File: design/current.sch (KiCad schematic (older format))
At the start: 4 parts

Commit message: Fixing connection errors
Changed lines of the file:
@@
 AR Path="/548DF2C8/55B3BD79/55B231D6" Ref="R30"  Part="1"
 AR Path="/548DF2C8/55B3BD84/55B231D6" Ref="R33"  Part="1"
-F 0 "R27" V 3605 2675 50  0000 C CNN
+F 0 "R33" V 3605 2675 50  0000 C CNN
 F 1 "22R" V 3525 2675 50  0000 C CNN
 F 2 "Resistors_SMD:R_0603" V 3455 2675 30  0001 C CNN
@@
 AR Path="/548DF2C8/55B3BD79/55B23207" Ref="R31"  Part="1"
 AR Path="/548DF2C8/55B3BD84/55B23207" Ref="R34"  Part="1"
-F 0 "R28" V 4080 2675 50  0000 C CNN
+F 0 "R34" V 4080 2675 50  0000 C CNN
 F 1 "10K" V 4000 2675 50  0000 C CNN
 F 2 "Resistors_SMD:R_0603" V 3930 2675 30  0001 C CNN
@@
 AR Path="/548DF2C8/55B3BD79/55B23290" Ref="R32"  Part="1"
 AR Path="/548DF2C8/55B3BD84/55B23290" Ref="R35"  Part="1"
-F 0 "R29" V 4080 3175 50  0000 C CNN
+F 0 "R35" V 4080 3175 50  0000 C CNN
 F 1 "10K" V 4000 3175 50  0000 C CNN
 F 2 "Resistors_SMD:R_0603" V 3930 3175 30  0001 C CNN
@@
 AR Path="/548DF2C8/55B3BD79/55B232D0" Ref="C6"  Part="1"
 AR Path="/548DF2C8/55B3BD84/55B232D0" Ref="C7"  Part="1"
-F 0 "C5" H 3550 3275 50  0000 L CNN
+F 0 "C7" H 3550 3275 50  0000 L CNN
 F 1 "10uF" H 3550 3075 50  0000 L CNN
 F 2 "Capacitors_SMD:C_0805" H 3563 3025 30  0001 C CNN
@@
 Connection ~ 4000 2875
 $Comp
-L GND #PWR053
+L GND #PWR054
 U 1 1 55B23417
 P 3525 3375
-AR Path="/548DF2C8/55B266EE/55B23417" Ref="#PWR053"  Part="1"
-AR Path="/548DF2C8/55B3A3F6/55B23417" Ref="#PWR055"  Part="1"
-AR Path="/548DF2C8/55B3A74F/55B23417" Ref="#PWR057"  Part="1"
-AR Path="/548DF2C8/55B3BD6E/55B23417" Ref="#PWR059"  Part="1"
-AR Path="/548DF2C8/55B3BD79/55B23417" Ref="#PWR061"  Part="1"
-AR Path="/548DF2C8/55B3BD84/55B23417" Ref="#PWR063"  Part="1"
-F 0 "#PWR059" H 3525 3125 50  0001 C CNN
+AR Path="/548DF2C8/55B266EE/55B23417" Ref="#PWR054"  Part="1"
+AR Path="/548DF2C8/55B3A3F6/55B23417" Ref="#PWR056"  Part="1"
+AR Path="/548DF2C8/55B3A74F/55B23417" Ref="#PWR058"  Part="1"
+AR Path="/548DF2C8/55B3BD6E/55B23417" Ref="#PWR060"  Part="1"
+AR Path="/548DF2C8/55B3BD79/55B23417" Ref="#PWR062"  Part="1"
+AR Path="/548DF2C8/55B3BD84/55B23417" Ref="#PWR064"  Part="1"
+F 0 "#PWR064" H 3525 3125 50  0001 C CNN
 F 1 "GND" H 3525 3225 50  0000 C CNN
 F 2 "" H 3525 3375 60  0000 C CNN
@@
 	4000 2525 4000 2475
 $Comp
-L +3.3V #PWR054
+L +3.3V #PWR055
 U 1 1 55B23695
 P 4000 2475
-AR Path="/548DF2C8/55B266EE/55B23695" Ref="#PWR054"  Part="1"
-AR Path="/548DF2C8/55B3A3F6/55B23695" Ref="#PWR056"  Part="1"
-AR Path="/548DF2C8/55B3A74F/55B23695" Ref="#PWR058"  Part="1"
-AR Path="/548DF2C8/55B3BD6E/55B23695" Ref="#PWR060"  Part="1"
-AR Path="/548DF2C8/55B3BD79/55B23695" Ref="#PWR062"  Part="1"
-AR Path="/548DF2C8/55B3BD84/55B23695" Ref="#PWR064"  Part="1"
-F 0 "#PWR060" H 4000 2325 50  0001 C CNN
+AR Path="/548DF2C8/55B266EE/55B23695" Ref="#PWR055"  Part="1"
+AR Path="/548DF2C8/55B3A3F6/55B23695" Ref="#PWR057"  Part="1"
+AR Path="/548DF2C8/55B3A74F/55B23695" Ref="#PWR059"  Part="1"
+AR Path="/548DF2C8/55B3BD6E/55B23695" Ref="#PWR061"  Part="1"
+AR Path="/548DF2C8/55B3BD79/55B23695" Ref="#PWR063"  Part="1"
+AR Path="/548DF2C8/55B3BD84/55B23695" Ref="#PWR065"  Part="1"
+F 0 "#PWR065" H 4000 2325 50  0001 C CNN
 F 1 "+3.3V" H 4000 2615 50  0000 C CNN
 F 2 "" H 4000 2475 60  0000 C CNN

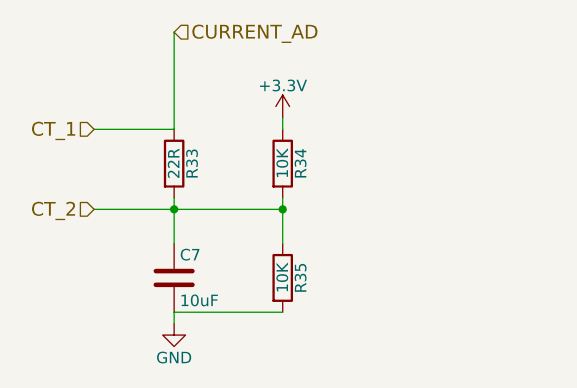
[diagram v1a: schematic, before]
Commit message: Agrego los dos circuitos extra para medir tension
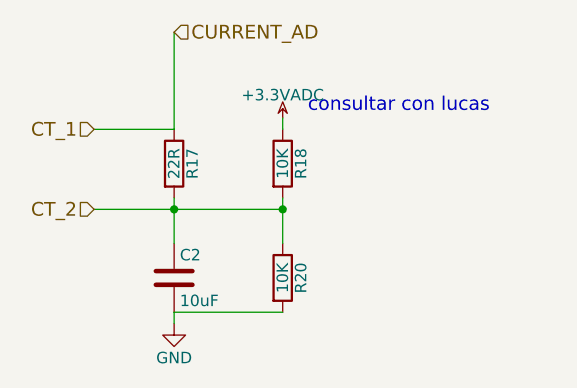
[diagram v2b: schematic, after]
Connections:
- net +3V3 renamed +3.3VADC
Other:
- note added: "consultar con lucas\n"
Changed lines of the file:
@@
 LIBS:memory
 LIBS:xilinx
-LIBS:special
 LIBS:microcontrollers
 LIBS:dsp
@@
 $Descr A4 11693 8268
 encoding utf-8
-Sheet 13 18
+Sheet 13 20
 Title "PIVI"
 Date "Mon 27 Jul 2015"
@@
 AR Path="/548DF2C8/55B3BD79/55B231D6" Ref="R30"  Part="1"
 AR Path="/548DF2C8/55B3BD84/55B231D6" Ref="R33"  Part="1"
-F 0 "R33" V 3605 2675 50  0000 C CNN
+F 0 "R17" V 3605 2675 50  0000 C CNN
 F 1 "22R" V 3525 2675 50  0000 C CNN
 F 2 "Resistors_SMD:R_0603" V 3455 2675 30  0001 C CNN
@@
 AR Path="/548DF2C8/55B3BD79/55B23207" Ref="R31"  Part="1"
 AR Path="/548DF2C8/55B3BD84/55B23207" Ref="R34"  Part="1"
-F 0 "R34" V 4080 2675 50  0000 C CNN
+F 0 "R18" V 4080 2675 50  0000 C CNN
 F 1 "10K" V 4000 2675 50  0000 C CNN
 F 2 "Resistors_SMD:R_0603" V 3930 2675 30  0001 C CNN
@@
 AR Path="/548DF2C8/55B3BD79/55B23290" Ref="R32"  Part="1"
 AR Path="/548DF2C8/55B3BD84/55B23290" Ref="R35"  Part="1"
-F 0 "R35" V 4080 3175 50  0000 C CNN
+F 0 "R20" V 4080 3175 50  0000 C CNN
 F 1 "10K" V 4000 3175 50  0000 C CNN
 F 2 "Resistors_SMD:R_0603" V 3930 3175 30  0001 C CNN
@@
 AR Path="/548DF2C8/55B3BD79/55B232D0" Ref="C6"  Part="1"
 AR Path="/548DF2C8/55B3BD84/55B232D0" Ref="C7"  Part="1"
-F 0 "C7" H 3550 3275 50  0000 L CNN
+F 0 "C2" H 3550 3275 50  0000 L CNN
 F 1 "10uF" H 3550 3075 50  0000 L CNN
 F 2 "Capacitors_SMD:C_0805" H 3563 3025 30  0001 C CNN
@@
 AR Path="/548DF2C8/55B3BD79/55B23417" Ref="#PWR062"  Part="1"
 AR Path="/548DF2C8/55B3BD84/55B23417" Ref="#PWR064"  Part="1"
-F 0 "#PWR064" H 3525 3125 50  0001 C CNN
+F 0 "#PWR054" H 3525 3125 50  0001 C CNN
 F 1 "GND" H 3525 3225 50  0000 C CNN
 F 2 "" H 3525 3375 60  0000 C CNN
@@
 Wire Wire Line
 	4000 2525 4000 2475
+Wire Wire Line
+	3525 3325 4000 3325
 $Comp
-L +3.3V #PWR055
-U 1 1 55B23695
+L +3.3VADC #PWR?
+U 1 1 55B9DD7E
 P 4000 2475
-AR Path="/548DF2C8/55B266EE/55B23695" Ref="#PWR055"  Part="1"
-AR Path="/548DF2C8/55B3A3F6/55B23695" Ref="#PWR057"  Part="1"
-AR Path="/548DF2C8/55B3A74F/55B23695" Ref="#PWR059"  Part="1"
-AR Path="/548DF2C8/55B3BD6E/55B23695" Ref="#PWR061"  Part="1"
-AR Path="/548DF2C8/55B3BD79/55B23695" Ref="#PWR063"  Part="1"
-AR Path="/548DF2C8/55B3BD84/55B23695" Ref="#PWR065"  Part="1"
-F 0 "#PWR065" H 4000 2325 50  0001 C CNN
-F 1 "+3.3V" H 4000 2615 50  0000 C CNN
+F 0 "#PWR?" H 4150 2425 50  0001 C CNN
+F 1 "+3.3VADC" H 4000 2575 50  0000 C CNN
 F 2 "" H 4000 2475 60  0000 C CNN
 F 3 "" H 4000 2475 60  0000 C CNN
@@
 	1    0    0    -1
 $EndComp
-Wire Wire Line
-	3525 3325 4000 3325
+Text Notes 4110 2457 0    60   ~ 0
+consultar con lucas\n
 $EndSCHEMATC

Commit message: Edito conexiones pinza, agregado debub uart, agregado tension referencia
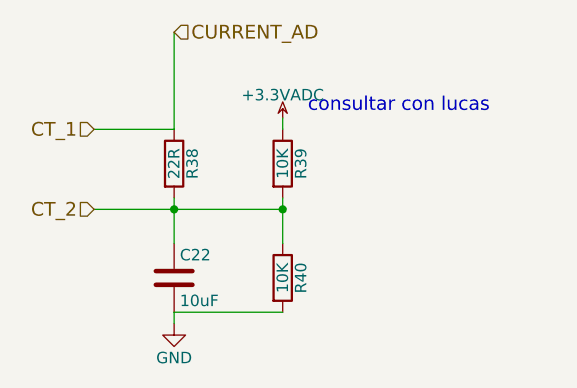
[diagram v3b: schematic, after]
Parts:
- renumbered C2 to C17, R17 to R23, R18 to R24, R20 to R25
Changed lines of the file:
@@
 CT_2
 $Comp
-L R R17
+L R R23
 U 1 1 55B231D6
 P 3525 2675
-AR Path="/548DF2C8/55B266EE/55B231D6" Ref="R17"  Part="1"
-AR Path="/548DF2C8/55B3A3F6/55B231D6" Ref="R21"  Part="1"
-AR Path="/548DF2C8/55B3A74F/55B231D6" Ref="R24"  Part="1"
-AR Path="/548DF2C8/55B3BD6E/55B231D6" Ref="R27"  Part="1"
-AR Path="/548DF2C8/55B3BD79/55B231D6" Ref="R30"  Part="1"
-AR Path="/548DF2C8/55B3BD84/55B231D6" Ref="R33"  Part="1"
-F 0 "R17" V 3605 2675 50  0000 C CNN
+AR Path="/548DF2C8/55B266EE/55B231D6" Ref="R23"  Part="1"
+AR Path="/548DF2C8/55B3A3F6/55B231D6" Ref="R26"  Part="1"
+AR Path="/548DF2C8/55B3A74F/55B231D6" Ref="R29"  Part="1"
+AR Path="/548DF2C8/55B3BD6E/55B231D6" Ref="R32"  Part="1"
+AR Path="/548DF2C8/55B3BD79/55B231D6" Ref="R35"  Part="1"
+AR Path="/548DF2C8/55B3BD84/55B231D6" Ref="R38"  Part="1"
+F 0 "R38" V 3605 2675 50  0000 C CNN
 F 1 "22R" V 3525 2675 50  0000 C CNN
 F 2 "Resistors_SMD:R_0603" V 3455 2675 30  0001 C CNN
@@
 $EndComp
 $Comp
-L R R18
+L R R24
 U 1 1 55B23207
 P 4000 2675
-AR Path="/548DF2C8/55B266EE/55B23207" Ref="R18"  Part="1"
-AR Path="/548DF2C8/55B3A3F6/55B23207" Ref="R22"  Part="1"
-AR Path="/548DF2C8/55B3A74F/55B23207" Ref="R25"  Part="1"
-AR Path="/548DF2C8/55B3BD6E/55B23207" Ref="R28"  Part="1"
-AR Path="/548DF2C8/55B3BD79/55B23207" Ref="R31"  Part="1"
-AR Path="/548DF2C8/55B3BD84/55B23207" Ref="R34"  Part="1"
-F 0 "R18" V 4080 2675 50  0000 C CNN
+AR Path="/548DF2C8/55B266EE/55B23207" Ref="R24"  Part="1"
+AR Path="/548DF2C8/55B3A3F6/55B23207" Ref="R27"  Part="1"
+AR Path="/548DF2C8/55B3A74F/55B23207" Ref="R30"  Part="1"
+AR Path="/548DF2C8/55B3BD6E/55B23207" Ref="R33"  Part="1"
+AR Path="/548DF2C8/55B3BD79/55B23207" Ref="R36"  Part="1"
+AR Path="/548DF2C8/55B3BD84/55B23207" Ref="R39"  Part="1"
+F 0 "R39" V 4080 2675 50  0000 C CNN
 F 1 "10K" V 4000 2675 50  0000 C CNN
 F 2 "Resistors_SMD:R_0603" V 3930 2675 30  0001 C CNN
@@
 $EndComp
 $Comp
-L R R20
+L R R25
 U 1 1 55B23290
 P 4000 3175
-AR Path="/548DF2C8/55B266EE/55B23290" Ref="R20"  Part="1"
-AR Path="/548DF2C8/55B3A3F6/55B23290" Ref="R23"  Part="1"
-AR Path="/548DF2C8/55B3A74F/55B23290" Ref="R26"  Part="1"
-AR Path="/548DF2C8/55B3BD6E/55B23290" Ref="R29"  Part="1"
-AR Path="/548DF2C8/55B3BD79/55B23290" Ref="R32"  Part="1"
-AR Path="/548DF2C8/55B3BD84/55B23290" Ref="R35"  Part="1"
-F 0 "R20" V 4080 3175 50  0000 C CNN
+AR Path="/548DF2C8/55B266EE/55B23290" Ref="R25"  Part="1"
+AR Path="/548DF2C8/55B3A3F6/55B23290" Ref="R28"  Part="1"
+AR Path="/548DF2C8/55B3A74F/55B23290" Ref="R31"  Part="1"
+AR Path="/548DF2C8/55B3BD6E/55B23290" Ref="R34"  Part="1"
+AR Path="/548DF2C8/55B3BD79/55B23290" Ref="R37"  Part="1"
+AR Path="/548DF2C8/55B3BD84/55B23290" Ref="R40"  Part="1"
+F 0 "R40" V 4080 3175 50  0000 C CNN
 F 1 "10K" V 4000 3175 50  0000 C CNN
 F 2 "Resistors_SMD:R_0603" V 3930 3175 30  0001 C CNN
@@
 $EndComp
 $Comp
-L C C2
+L C C17
 U 1 1 55B232D0
 P 3525 3175
-AR Path="/548DF2C8/55B266EE/55B232D0" Ref="C2"  Part="1"
-AR Path="/548DF2C8/55B3A3F6/55B232D0" Ref="C3"  Part="1"
-AR Path="/548DF2C8/55B3A74F/55B232D0" Ref="C4"  Part="1"
-AR Path="/548DF2C8/55B3BD6E/55B232D0" Ref="C5"  Part="1"
-AR Path="/548DF2C8/55B3BD79/55B232D0" Ref="C6"  Part="1"
-AR Path="/548DF2C8/55B3BD84/55B232D0" Ref="C7"  Part="1"
-F 0 "C2" H 3550 3275 50  0000 L CNN
+AR Path="/548DF2C8/55B266EE/55B232D0" Ref="C17"  Part="1"
+AR Path="/548DF2C8/55B3A3F6/55B232D0" Ref="C18"  Part="1"
+AR Path="/548DF2C8/55B3A74F/55B232D0" Ref="C19"  Part="1"
+AR Path="/548DF2C8/55B3BD6E/55B232D0" Ref="C20"  Part="1"
+AR Path="/548DF2C8/55B3BD79/55B232D0" Ref="C21"  Part="1"
+AR Path="/548DF2C8/55B3BD84/55B232D0" Ref="C22"  Part="1"
+F 0 "C22" H 3550 3275 50  0000 L CNN
 F 1 "10uF" H 3550 3075 50  0000 L CNN
 F 2 "Capacitors_SMD:C_0805" H 3563 3025 30  0001 C CNN
@@
 Connection ~ 4000 2875
 $Comp
-L GND #PWR054
+L GND #PWR52
 U 1 1 55B23417
 P 3525 3375
-AR Path="/548DF2C8/55B266EE/55B23417" Ref="#PWR054"  Part="1"
-AR Path="/548DF2C8/55B3A3F6/55B23417" Ref="#PWR056"  Part="1"
-AR Path="/548DF2C8/55B3A74F/55B23417" Ref="#PWR058"  Part="1"
-AR Path="/548DF2C8/55B3BD6E/55B23417" Ref="#PWR060"  Part="1"
-AR Path="/548DF2C8/55B3BD79/55B23417" Ref="#PWR062"  Part="1"
-AR Path="/548DF2C8/55B3BD84/55B23417" Ref="#PWR064"  Part="1"
-F 0 "#PWR054" H 3525 3125 50  0001 C CNN
+AR Path="/548DF2C8/55B266EE/55B23417" Ref="#PWR52"  Part="1"
+AR Path="/548DF2C8/55B3A3F6/55B23417" Ref="#PWR54"  Part="1"
+AR Path="/548DF2C8/55B3A74F/55B23417" Ref="#PWR56"  Part="1"
+AR Path="/548DF2C8/55B3BD6E/55B23417" Ref="#PWR58"  Part="1"
+AR Path="/548DF2C8/55B3BD79/55B23417" Ref="#PWR60"  Part="1"
+AR Path="/548DF2C8/55B3BD84/55B23417" Ref="#PWR62"  Part="1"
+F 0 "#PWR62" H 3525 3125 50  0001 C CNN
 F 1 "GND" H 3525 3225 50  0000 C CNN
 F 2 "" H 3525 3375 60  0000 C CNN
@@
 	3525 3325 4000 3325
 $Comp
-L +3.3VADC #PWR?
+L +3.3VADC #PWR53
 U 1 1 55B9DD7E
 P 4000 2475
-F 0 "#PWR?" H 4150 2425 50  0001 C CNN
+AR Path="/548DF2C8/55B266EE/55B9DD7E" Ref="#PWR53"  Part="1"
+AR Path="/548DF2C8/55B3A3F6/55B9DD7E" Ref="#PWR55"  Part="1"
+AR Path="/548DF2C8/55B3A74F/55B9DD7E" Ref="#PWR57"  Part="1"
+AR Path="/548DF2C8/55B3BD6E/55B9DD7E" Ref="#PWR59"  Part="1"
+AR Path="/548DF2C8/55B3BD79/55B9DD7E" Ref="#PWR61"  Part="1"
+AR Path="/548DF2C8/55B3BD84/55B9DD7E" Ref="#PWR63"  Part="1"
+F 0 "#PWR63" H 4150 2425 50  0001 C CNN
 F 1 "+3.3VADC" H 4000 2575 50  0000 C CNN
 F 2 "" H 4000 2475 60  0000 C CNN
